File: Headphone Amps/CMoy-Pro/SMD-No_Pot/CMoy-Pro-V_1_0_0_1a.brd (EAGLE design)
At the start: 39.2 x 28.9 mm, 20 parts, among them IC1 AD8620R, X1 STEREOJACK, X2 STEREOJACK

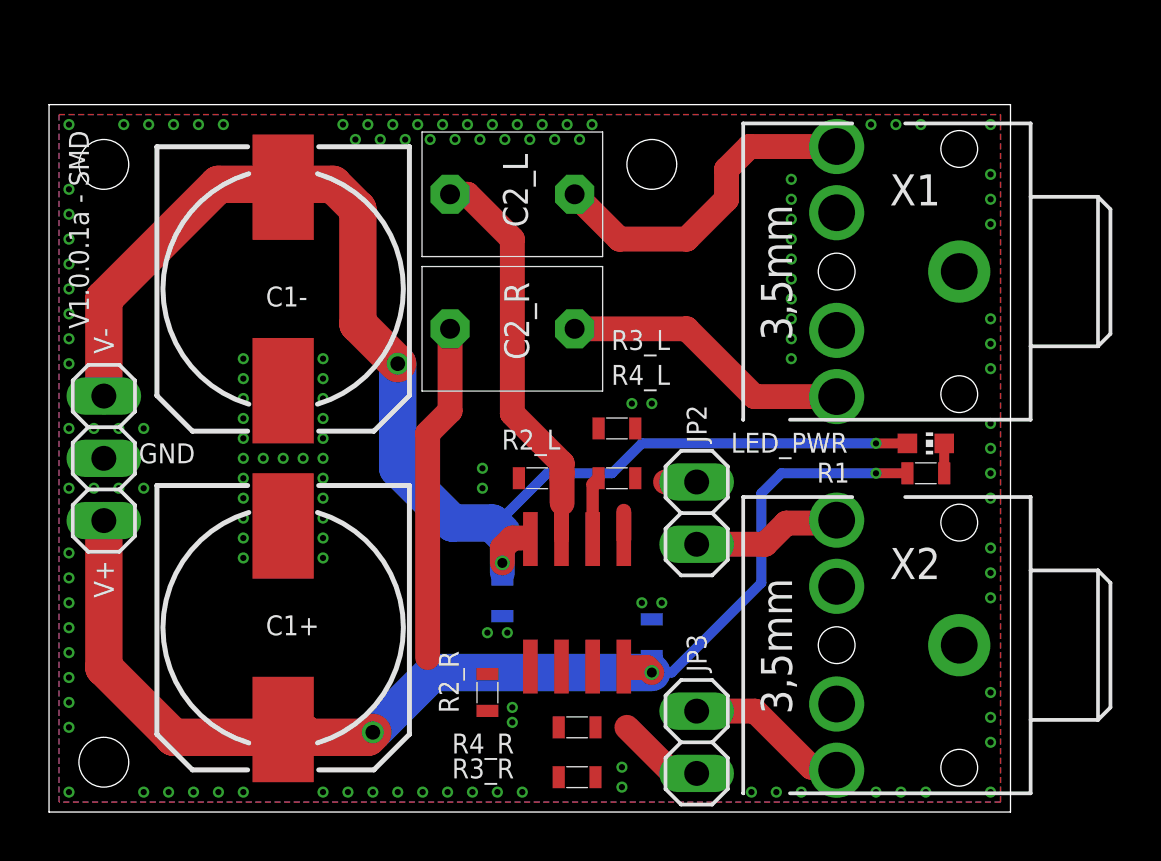
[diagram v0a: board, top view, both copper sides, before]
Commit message: Changes from surface book
These are the files that have changed on the surface book. I have not tracked the project individually.
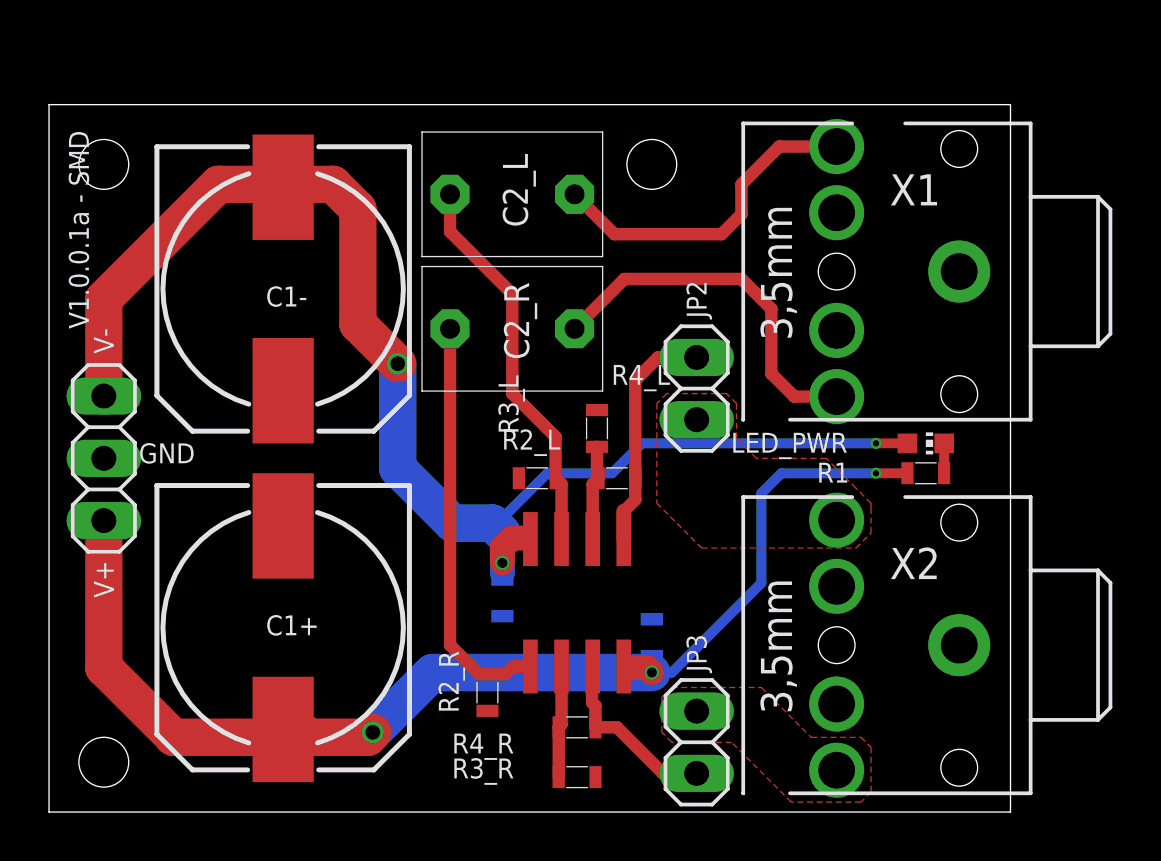
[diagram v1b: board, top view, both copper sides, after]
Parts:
- moved JP2 5.08 mm to (26.4, 17.3)
- moved R3_L 0.81 mm to (22.4, 15.6), turned to 270 degrees
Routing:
- net OUT_L: track 2.40 -> 9.56 mm
- net N$3: track 6.71 -> 0.00 mm
- net N$2: track 6.12 -> 0.00 mm
- net N$6: track 0.00 -> 4.56 mm
- net OUT_R: track 3.62 -> 7.45 mm
- net HP_L: track 11.8 -> 15.1 mm
- net IN_L: track 13.9 -> 16.9 mm
- net N$5: track 2.58 -> 3.89 mm
- net IN_R: track 16.8 -> 15.9 mm
- added copper zone on layer 1, net N$2
- added copper zone on layer 1, net N$3
- removed copper zone on layer 1, net GND
- removed copper zone on layer 16, net GND
